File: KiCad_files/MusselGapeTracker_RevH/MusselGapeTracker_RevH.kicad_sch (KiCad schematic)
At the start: 83 parts, among them J1 AVR_SPI_PRG_6PTH, U1 ATMEGA328P, U2 DS3231M+TRL, U3 DS3231MZ

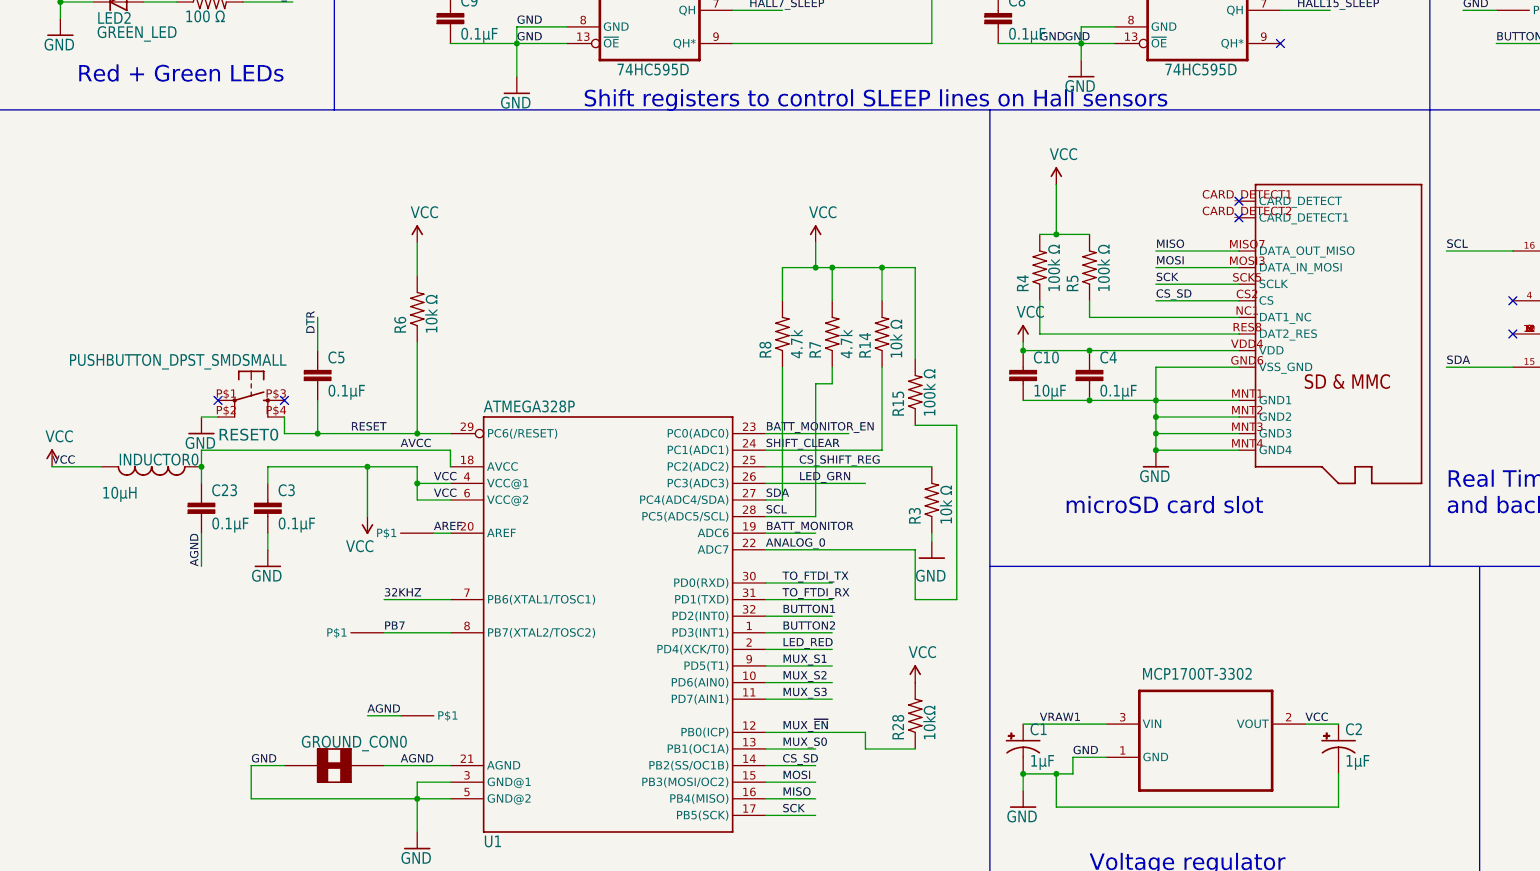
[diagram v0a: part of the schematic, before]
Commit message: replace Molex 502774-0891 with GCT MEM2052-00-195-00-A
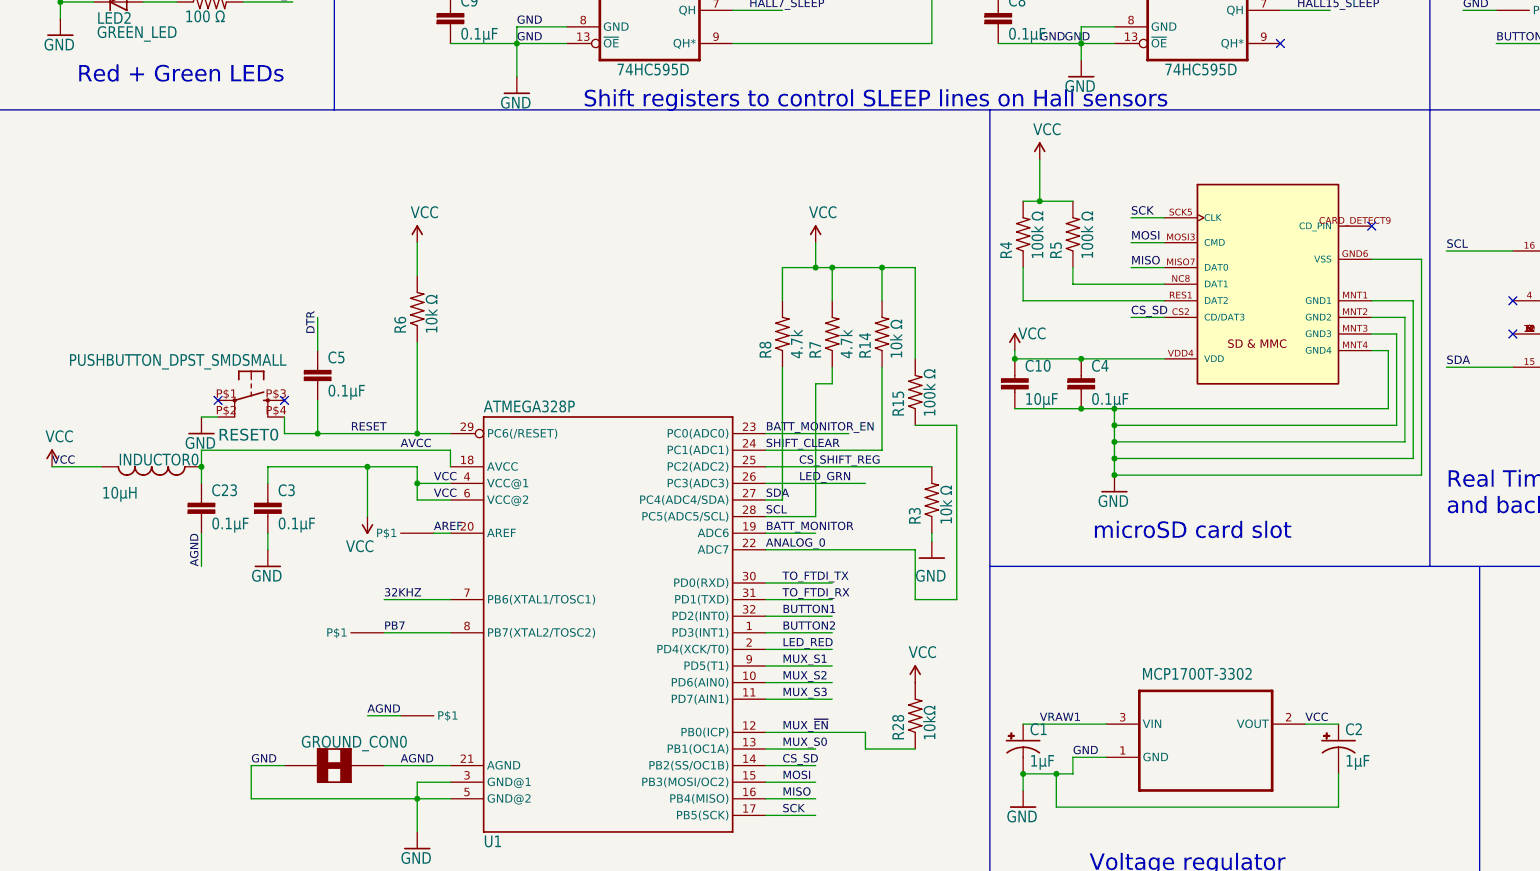
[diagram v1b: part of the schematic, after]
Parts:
- SD1: renamed from U$1; value MICROSD_MOLEX_REVERSECURRENT -> GCT_MEM2052-00-195-00-A_REVA; footprint MusselGapeTracker_RevE:MICROSD_SOCKET_MOLEX_REVERSEMOUNT -> MusselGapeTracker_RevH:GCT_MEM2052-00-195-00-A_REVA; symbol MusselGapeTracker_RevE-eagle-import:MICROSD_MOLEX_REVERSECURRENT -> MusselGapeTracker_RevH-SlaterSymbols:MEM2052-00-195-00-A_REVA; Availability (none) -> In Stock; Check_prices (none) -> https://www.snapeda.com/parts/MEM2052-00-195-00-A/Global+Co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; Description_1 (none) -> MicroSD Push push Memory Card Connector; MANUFACTURER (none) -> Global Connector Technology; MAXIMUM_PACKAGE_HEIGHT (none) -> 1.95 mm; MF (none) -> Global Connector Technology; MP (none) -> MEM2052-00-195-00-A; PARTREV (none) -> A; Package (none) -> None; Price (none) -> None; Purchase-URL (none) -> https://www.snapeda.com/api/url_track_click_mouser/?unipart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; SNAPEDA_PN (none) -> MEM2052-00-195-00-A; STANDARD (none) -> Manufacturer Recommendations; SnapEDA_Link (none) -> https://www.snapeda.com/parts/MEM2052-00-195-00-A/Global+Co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
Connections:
- net at R4.1: now also SD1.RES1 (DAT2); no longer SD1.RES8 (DAT2_RES)
- net at R5.1: now also SD1.NC8 (DAT1); no longer SD1.NC1 (DAT1_NC)
- no-connect marks 15 -> 14
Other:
- moved on the sheet: C10, C4, R4, R5

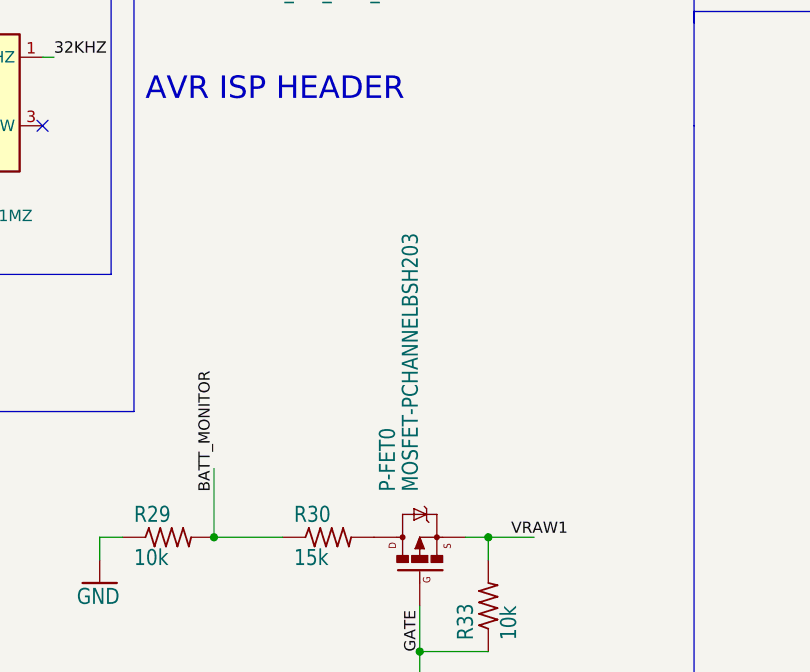
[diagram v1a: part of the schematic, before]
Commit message: Update p-channel mosfet from BSH203 to SSM3J328R
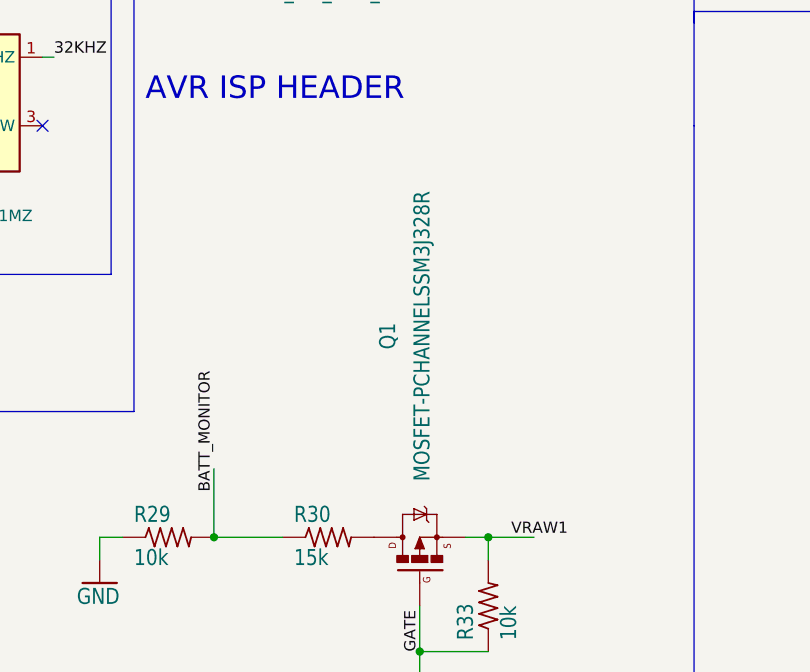
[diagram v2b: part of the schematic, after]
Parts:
- removed P-FET0: MOSFET-PCHANNELBSH203, MusselGapeTracker_RevE:SOT23-3, symbol MusselGapeTracker_RevE-eagle-import:MOSFET-PCHANNELBSH203
- added Q1: MOSFET-PCHANNELSSM3J328R, MusselGapeTracker_RevE:SOT23-3, symbol MusselGapeTracker_RevE-eagle-import:MOSFET-PCHANNELSSM3J328R
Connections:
- net GATE: now also Q1.1 (G)
- net VRAW1: now also Q1.2 (S)
- net at R30.2: now also Q1.3 (D)
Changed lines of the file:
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@@
+	)
+	(symbol
+		(lib_id "MusselGapeTracker_RevE-eagle-import:MOSFET-PCHANNELSSM3J328R")
+		(at 353.06 417.83 90)
+		(unit 1)
+		(exclude_from_sim no)
+		(in_bom yes)
+		(on_board yes)
+		(dnp no)
+		(property "Reference" "Q1"
+			(at 349.504 395.478 0)
+			(effects
+				(font
+					(size 1.778 1.5113)
+				)
+			)
+		)
+		(property "Value" "MOSFET-PCHANNELSSM3J328R"
+			(at 353.314 395.478 0)
+			(effects
+				(font
+					(size 1.778 1.5113)
+				)
+			)
+		)
+		(property "Footprint" "MusselGapeTracker_RevE:SOT23-3"
+			(at 353.06 417.83 0)
+			(effects
+				(font
+					(size 1.27 1.27)
+				)
+				(hide yes)
+			)
+		)
+		(property "Datasheet" ""
+			(at 353.06 417.83 0)
+			(effects
+				(font
+					(size 1.27 1.27)
+				)
+				(hide yes)
+			)
+		)
+		(property "Description" ""
+			(at 353.06 417.83 0)
+			(effects
+				(font
+					(size 1.27 1.27)
+				)
+				(hide yes)
+			)
+		)
+		(pin "1"
+		)
+		(pin "3"
+		)
+		(pin "2"
+		)
+		(instances
+			(project ""
+				(path "/16a6d501-f88c-4776-88ce-bd33e196cf14"
+					(reference "Q1")
+					(unit 1)
+				)
+			)
+		)
 	)
 	(symbol
@@
 					(unit 1)
 				)
-			)
-		)
-	)
-	(symbol
-		(lib_id "MusselGapeTracker_RevE-eagle-import:MOSFET-PCHANNELBSH203")
-		(at 353.06 417.83 90)
-		(unit 1)
-		(exclude_from_sim no)
-		(in_bom yes)
-		(on_board yes)
-		(dnp no)
-		(property "Reference" "P-FET0"
-			(at 350.52 412.75 0)
-			(effects
-				(font
-					(size 1.778 1.5113)
-				)
-				(justify left bottom)
-			)
-		)
-		(property "Value" "MOSFET-PCHANNELBSH203"
-			(at 353.06 412.75 0)
-			(effects
-				(font
-					(size 1.778 1.5113)
-				)
-				(justify left bottom)
-			)
-		)
-		(property "Footprint" "MusselGapeTracker_RevE:SOT23-3"
-			(at 353.06 417.83 0)
-			(effects
-				(font
-					(size 1.27 1.27)
-				)
-				(hide yes)
-			)
-		)
-		(property "Datasheet" ""
-			(at 353.06 417.83 0)
-			(effects
-				(font
-					(size 1.27 1.27)
-				)
-				(hide yes)
-			)
-		)
-		(property "Description" ""
-			(at 353.06 417.83 0)
-			(effects
-				(font
-					(size 1.27 1.27)
-				)
-			)
-		)
-		(pin "1"
-		)
-		(pin "2"
-		)
-		(pin "3"
-		)
-		(instances
-			(project "MusselGapeTracker_RevH"
-				(path "/16a6d501-f88c-4776-88ce-bd33e196cf14"
-					(reference "P-FET0")
-					(unit 1)
-				)
